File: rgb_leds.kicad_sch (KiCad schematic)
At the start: 11 parts

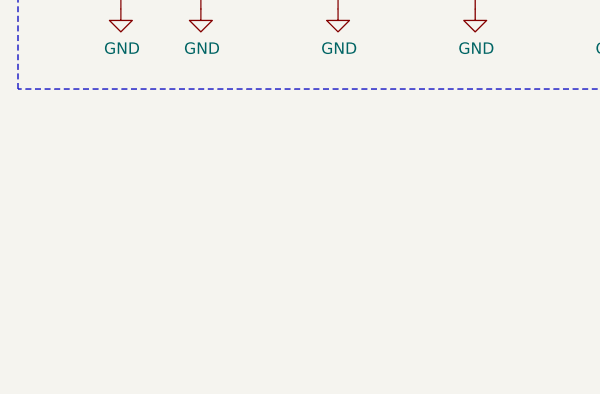
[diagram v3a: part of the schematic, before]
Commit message: Finish the board redesign with SoM on the bottom
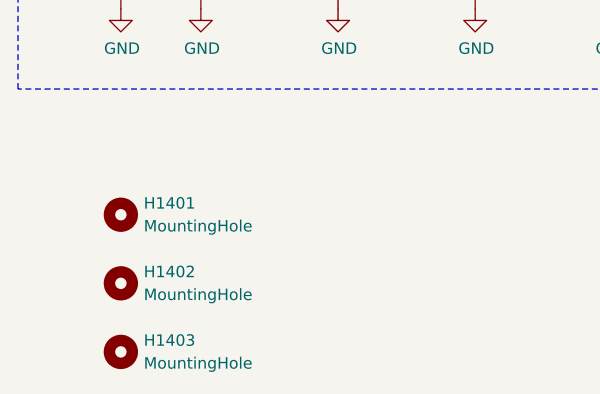
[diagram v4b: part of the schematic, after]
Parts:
- added H1401, H1402, H1403: MountingHole, MountingHole:MountingHole_3.2mm_M3, symbol Mechanical:MountingHole
- LED1401, LED1402, LED1403, LED1404, LED1405: footprint Hatlabs:LED-SMD_4P-L4.0-W1.4_SK6805SIDE-S -> Hatlabs:LED_WS2812E-4020_PLCC4_4.0x2.0mm_P0.85mm
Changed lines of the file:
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@@
 			)
 		)
-		(property "Datasheet" "https://search.murata.co.jp/Ceramy/image/img/A01X/G101/ENG/GRM155R71C104KA88-01.pdf"
+		(property "Datasheet" "~"
 			(at 121.92 120.65 0)
 			(effects
@@
 			)
 		)
-		(property "Description" ""
+		(property "Description" "Unpolarized capacitor"
 			(at 121.92 120.65 0)
 			(effects
@@
 				(path "/abc482bd-3f17-4d35-80db-1da3dcdb5c27/850df4bf-e40a-4082-adc2-76804638b949/7441bc5f-8874-43c2-af8a-50459ea25028"
 					(reference "C1403")
+					(unit 1)
+				)
+			)
+		)
+	)
+	(symbol
+		(lib_id "Mechanical:MountingHole")
+		(at 97.79 154.94 0)
+		(unit 1)
+		(exclude_from_sim no)
+		(in_bom no)
+		(on_board yes)
+		(dnp no)
+		(fields_autoplaced yes)
+		(property "Reference" "H1402"
+			(at 100.33 153.6699 0)
+			(effects
+				(font
+					(size 1.27 1.27)
+				)
+				(justify left)
+			)
+		)
+		(property "Value" "MountingHole"
+			(at 100.33 156.2099 0)
+			(effects
+				(font
+					(size 1.27 1.27)
+				)
+				(justify left)
+			)
+		)
+		(property "Footprint" "MountingHole:MountingHole_3.2mm_M3"
+			(at 97.79 154.94 0)
+			(effects
+				(font
+					(size 1.27 1.27)
+				)
+				(hide yes)
+			)
+		)
+		(property "Datasheet" "~"
+			(at 97.79 154.94 0)
+			(effects
+				(font
+					(size 1.27 1.27)
+				)
+				(hide yes)
+			)
+		)
+		(property "Description" "Mounting Hole without connection"
+			(at 97.79 154.94 0)
+			(effects
+				(font
+					(size 1.27 1.27)
+				)
+				(hide yes)
+			)
+		)
+		(instances
+			(project "HALPI2"
+				(path "/abc482bd-3f17-4d35-80db-1da3dcdb5c27/850df4bf-e40a-4082-adc2-76804638b949/7441bc5f-8874-43c2-af8a-50459ea25028"
+					(reference "H1402")
 					(unit 1)
 				)
@@
 			)
 		)
-		(property "Datasheet" "https://search.murata.co.jp/Ceramy/image/img/A01X/G101/ENG/GRM155R71C104KA88-01.pdf"
+		(property "Datasheet" "~"
 			(at 152.4 120.65 0)
 			(effects
@@
 			)
 		)
-		(property "Description" ""
+		(property "Description" "Unpolarized capacitor"
 			(at 152.4 120.65 0)
 			(effects
@@
 			)
 		)
-		(property "Datasheet" "https://search.murata.co.jp/Ceramy/image/img/A01X/G101/ENG/GRM155R71C104KA88-01.pdf"
+		(property "Datasheet" "~"
 			(at 137.16 120.65 0)
 			(effects
@@
 			)
 		)
-		(property "Description" ""
+		(property "Description" "Unpolarized capacitor"
 			(at 137.16 120.65 0)
 			(effects
@@
 			)
 		)
-		(property "Datasheet" ""
+		(property "Datasheet" "~"
 			(at 97.79 120.65 0)
 			(effects
@@
 			)
 		)
-		(property "Description" ""
+		(property "Description" "Unpolarized capacitor"
 			(at 97.79 120.65 0)
 			(effects
@@
 				(path "/abc482bd-3f17-4d35-80db-1da3dcdb5c27/850df4bf-e40a-4082-adc2-76804638b949/7441bc5f-8874-43c2-af8a-50459ea25028"
 					(reference "C1401")
+					(unit 1)
+				)
+			)
+		)
+	)
+	(symbol
+		(lib_id "Mechanical:MountingHole")
+		(at 97.79 147.32 0)
+		(unit 1)
+		(exclude_from_sim no)
+		(in_bom no)
+		(on_board yes)
+		(dnp no)
+		(fields_autoplaced yes)
+		(property "Reference" "H1401"
+			(at 100.33 146.0499 0)
+			(effects
+				(font
+					(size 1.27 1.27)
+				)
+				(justify left)
+			)
+		)
+		(property "Value" "MountingHole"
+			(at 100.33 148.5899 0)
+			(effects
+				(font
+					(size 1.27 1.27)
+				)
+				(justify left)
+			)
+		)
+		(property "Footprint" "MountingHole:MountingHole_3.2mm_M3"
+			(at 97.79 147.32 0)
+			(effects
+				(font
+					(size 1.27 1.27)
+				)
+				(hide yes)
+			)
+		)
+		(property "Datasheet" "~"
+			(at 97.79 147.32 0)
+			(effects
+				(font
+					(size 1.27 1.27)
+				)
+				(hide yes)
+			)
+		)
+		(property "Description" "Mounting Hole without connection"
+			(at 97.79 147.32 0)
+			(effects
+				(font
+					(size 1.27 1.27)
+				)
+				(hide yes)
+			)
+		)
+		(instances
+			(project ""
+				(path "/abc482bd-3f17-4d35-80db-1da3dcdb5c27/850df4bf-e40a-4082-adc2-76804638b949/7441bc5f-8874-43c2-af8a-50459ea25028"
+					(reference "H1401")
 					(unit 1)
 				)
@@
 			)
 		)
-		(property "Footprint" "Hatlabs:LED-SMD_4P-L4.0-W1.4_SK6805SIDE-S"
+		(property "Footprint" "Hatlabs:LED_WS2812E-4020_PLCC4_4.0x2.0mm_P0.85mm"
 			(at 125.73 100.33 0)
 			(effects
@@
 			)
 		)
-		(property "Datasheet" "https://www.lcsc.com/datasheet/lcsc_datasheet_2110250930_OPSCO-Optoelectronics-SK6805MICRO-J_C2909056.pdf"
+		(property "Datasheet" "https://cdn-shop.adafruit.com/datasheets/WS2812B.pdf"
 			(at 120.65 100.33 0)
 			(effects
@@
 			)
 		)
-		(property "Footprint" "Hatlabs:LED-SMD_4P-L4.0-W1.4_SK6805SIDE-S"
+		(property "Footprint" "Hatlabs:LED_WS2812E-4020_PLCC4_4.0x2.0mm_P0.85mm"
 			(at 156.21 100.33 0)
 			(effects
@@
 			)
 		)
-		(property "Datasheet" "https://www.lcsc.com/datasheet/lcsc_datasheet_2110250930_OPSCO-Optoelectronics-SK6805MICRO-J_C2909056.pdf"
+		(property "Datasheet" "https://cdn-shop.adafruit.com/datasheets/WS2812B.pdf"
 			(at 151.13 100.33 0)
 			(effects
@@
 			)
 		)
-		(property "Datasheet" "https://search.murata.co.jp/Ceramy/image/img/A01X/G101/ENG/GRM155R71C104KA88-01.pdf"
+		(property "Datasheet" "~"
 			(at 167.64 120.65 0)
 			(effects
@@
 			)
 		)
-		(property "Description" ""
+		(property "Description" "Unpolarized capacitor"
 			(at 167.64 120.65 0)
 			(effects
@@
 			)
 		)
-		(property "Datasheet" "https://search.murata.co.jp/Ceramy/image/img/A01X/G101/ENG/GRM155R71C104KA88-01.pdf"
+		(property "Datasheet" "~"
 			(at 106.68 120.65 0)
 			(effects
@@
 			)
 		)
-		(property "Description" ""
+		(property "Description" "Unpolarized capacitor"
 			(at 106.68 120.65 0)
 			(effects
@@
 			)
 		)
-		(property "Footprint" "Hatlabs:LED-SMD_4P-L4.0-W1.4_SK6805SIDE-S"
+		(property "Footprint" "Hatlabs:LED_WS2812E-4020_PLCC4_4.0x2.0mm_P0.85mm"
 			(at 140.97 100.33 0)
 			(effects
@@
 			)
 		)
-		(property "Datasheet" "https://www.lcsc.com/datasheet/lcsc_datasheet_2110250930_OPSCO-Optoelectronics-SK6805MICRO-J_C2909056.pdf"
+		(property "Datasheet" "https://cdn-shop.adafruit.com/datasheets/WS2812B.pdf"
 			(at 135.89 100.33 0)
 			(effects
@@
 			)
 		)
-		(property "Footprint" "Hatlabs:LED-SMD_4P-L4.0-W1.4_SK6805SIDE-S"
+		(property "Footprint" "Hatlabs:LED_WS2812E-4020_PLCC4_4.0x2.0mm_P0.85mm"
 			(at 171.45 100.33 0)
 			(effects
@@
 			)
 		)
-		(property "Datasheet" "https://www.lcsc.com/datasheet/lcsc_datasheet_2110250930_OPSCO-Optoelectronics-SK6805MICRO-J_C2909056.pdf"
+		(property "Datasheet" "https://cdn-shop.adafruit.com/datasheets/WS2812B.pdf"
 			(at 166.37 100.33 0)
 			(effects
@@
 			)
 		)
-		(property "Footprint" "Hatlabs:LED-SMD_4P-L4.0-W1.4_SK6805SIDE-S"
+		(property "Footprint" "Hatlabs:LED_WS2812E-4020_PLCC4_4.0x2.0mm_P0.85mm"
 			(at 110.49 100.33 0)
 			(effects
@@
 			)
 		)
-		(property "Datasheet" "https://www.lcsc.com/datasheet/lcsc_datasheet_2110250930_OPSCO-Optoelectronics-SK6805MICRO-J_C2909056.pdf"
+		(property "Datasheet" "https://cdn-shop.adafruit.com/datasheets/WS2812B.pdf"
 			(at 105.41 100.33 0)
 			(effects
@@
 					(unit 1)
 				)
+			)
+		)
+	)
+	(symbol
+		(lib_id "Mechanical:MountingHole")
+		(at 97.79 162.56 0)
+		(unit 1)
+		(exclude_from_sim no)
+		(in_bom no)
+		(on_board yes)
+		(dnp no)
+		(fields_autoplaced yes)
+		(property "Reference" "H1403"
+			(at 100.33 161.2899 0)
+			(effects
+				(font
+					(size 1.27 1.27)
+				)
+				(justify left)
+			)
+		)
+		(property "Value" "MountingHole"
+			(at 100.33 163.8299 0)
+			(effects
+				(font
+					(size 1.27 1.27)
+				)
+				(justify left)
+			)
+		)
+		(property "Footprint" "MountingHole:MountingHole_3.2mm_M3"
+			(at 97.79 162.56 0)
+			(effects
+				(font
+					(size 1.27 1.27)
+				)
+				(hide yes)
+			)
+		)
+		(property "Datasheet" "~"
+			(at 97.79 162.56 0)
+			(effects
+				(font
+					(size 1.27 1.27)
+				)
+				(hide yes)
+			)
+		)
+		(property "Description" "Mounting Hole without connection"
+			(at 97.79 162.56 0)
+			(effects
+				(font
+					(size 1.27 1.27)
+				)
+				(hide yes)
+			)
+		)
+		(instances
+			(project "HALPI2"
+				(path "/abc482bd-3f17-4d35-80db-1da3dcdb5c27/850df4bf-e40a-4082-adc2-76804638b949/7441bc5f-8874-43c2-af8a-50459ea25028"
+					(reference "H1403")
+					(unit 1)
+				)

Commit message: Further refinements
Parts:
- added TP1207: TestPoint, TestPoint:TestPoint_Pad_D1.0mm, symbol Connector:TestPoint
- LED1401, LED1402, LED1403, LED1404, LED1405: value SK6805MICRO-J -> SK6805SIDE-G-003; footprint Hatlabs:LED_WS2812E-4020_PLCC4_4.0x2.0mm_P0.85mm -> Hatlabs:LED-SMD_4P-L3.5-W1.55_SK6805SIDE-G; symbol Hatlabs:Worldsemi_WS2812E-4020 -> Hatlabs:SK6805SIDE-G; LCSC C2909057 -> C31452139
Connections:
- net +5V: now also LED1401.3 (VCC), LED1402.3 (VCC), LED1403.3 (VCC), LED1404.3 (VCC), LED1405.3 (VCC); no longer LED1401.1 (VCC), LED1402.1 (VCC), LED1403.1 (VCC), LED1404.1 (VCC), LED1405.1 (VCC)
- net DIN2: now also LED1401.1 (DOUT); no longer LED1401.2 (DOUT)
- net DIN3: now also LED1402.1 (DOUT); no longer LED1402.2 (DOUT)
- net DIN4: now also LED1403.1 (DOUT); no longer LED1403.2 (DOUT)
- net DIN5: now also LED1404.1 (DOUT); no longer LED1404.2 (DOUT)
- net GND: now also LED1401.2 (GND), LED1402.2 (GND), LED1403.2 (GND), LED1404.2 (GND), LED1405.2 (GND); no longer LED1401.3 (GND), LED1402.3 (GND), LED1403.3 (GND), LED1404.3 (GND), LED1405.3 (GND)
- new net DOUT: LED1405.1 (DOUT), TP1207.1
- no-connect marks 1 -> 0

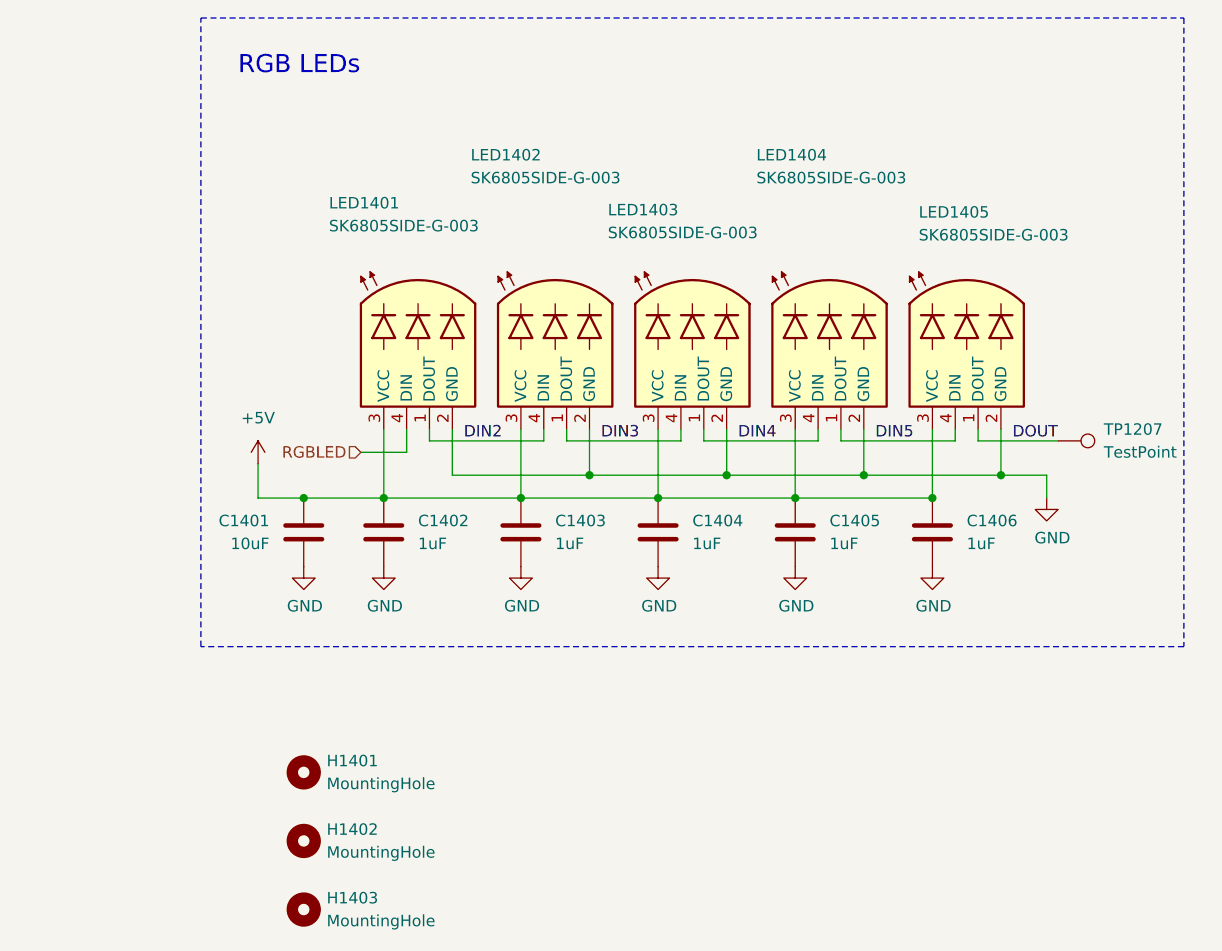
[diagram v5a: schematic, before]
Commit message: Finish transitioning to RP2040
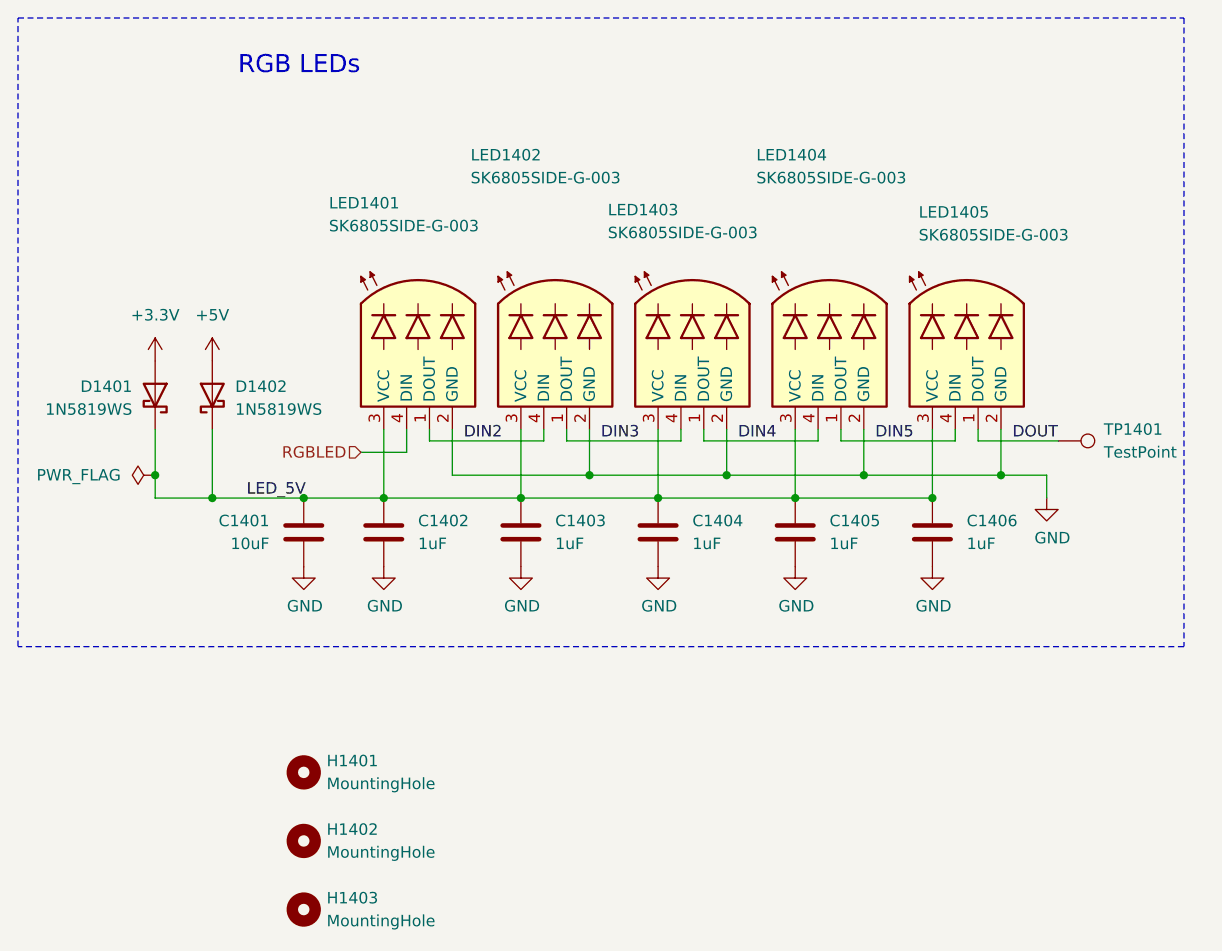
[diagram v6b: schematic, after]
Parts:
- added D1401, D1402: 1N5819WS, Diode_SMD:D_SOD-323, symbol Device:D_Schottky
- renumbered TP1207 to TP1401
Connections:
- net +5V: now also D1402.2 (A); no longer C1401.1, C1402.1, C1403.1, C1404.1, C1405.1, C1406.1, LED1401.3 (VCC), LED1402.3 (VCC), LED1403.3 (VCC), LED1404.3 (VCC), LED1405.3 (VCC)
- new net +3.3V: D1401.2 (A)
- new net LED_5V: C1401.1, C1402.1, C1403.1, C1404.1, C1405.1, C1406.1, D1401.1 (K), D1402.1 (K), LED1401.3 (VCC), LED1402.3 (VCC), LED1403.3 (VCC), LED1404.3 (VCC), LED1405.3 (VCC)

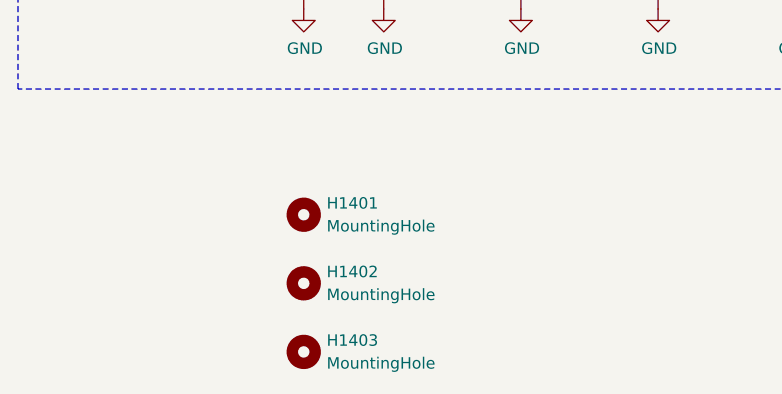
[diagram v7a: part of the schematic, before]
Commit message: Update the design to match the enclosure changes
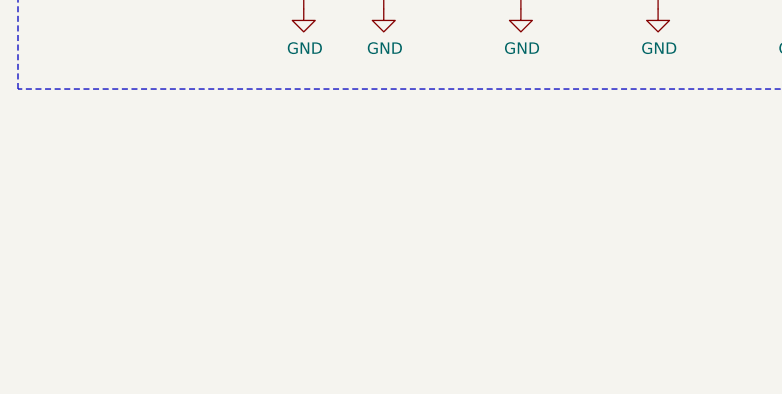
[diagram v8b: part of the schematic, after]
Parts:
- removed H1401, H1402, H1403: MountingHole, MountingHole:MountingHole_3.2mm_M3, symbol Mechanical:MountingHole
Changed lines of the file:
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@@
 	(title_block
 		(title "HALPI2")
-		(date "2025-02-26")
-		(rev "v0.1.0")
+		(date "2025-03-27")
+		(rev "v0.2.0")
 		(company "Hat Labs Oy")
 		(comment 1 "https://ohwr.org/cern_ohl_s_v2.pdf")
@@
 	)
 	(symbol
-		(lib_id "Mechanical:MountingHole")
-		(at 97.79 154.94 0)
-		(unit 1)
-		(exclude_from_sim no)
-		(in_bom no)
-		(on_board yes)
-		(dnp no)
-		(fields_autoplaced yes)
-		(property "Reference" "H1402"
-			(at 100.33 153.6699 0)
-			(effects
-				(font
-					(size 1.27 1.27)
-				)
-				(justify left)
-			)
-		)
-		(property "Value" "MountingHole"
-			(at 100.33 156.2099 0)
-			(effects
-				(font
-					(size 1.27 1.27)
-				)
-				(justify left)
-			)
-		)
-		(property "Footprint" "MountingHole:MountingHole_3.2mm_M3"
-			(at 97.79 154.94 0)
-			(effects
-				(font
-					(size 1.27 1.27)
-				)
-				(hide yes)
-			)
-		)
-		(property "Datasheet" "~"
-			(at 97.79 154.94 0)
-			(effects
-				(font
-					(size 1.27 1.27)
-				)
-				(hide yes)
-			)
-		)
-		(property "Description" "Mounting Hole without connection"
-			(at 97.79 154.94 0)
-			(effects
-				(font
-					(size 1.27 1.27)
-				)
-				(hide yes)
-			)
-		)
-		(property "LCSC Part" ""
-			(at 97.79 154.94 0)
-			(effects
-				(font
-					(size 1.27 1.27)
-				)
-			)
-		)
-		(instances
-			(project "HALPI2"
-				(path "/abc482bd-3f17-4d35-80db-1da3dcdb5c27/850df4bf-e40a-4082-adc2-76804638b949/7441bc5f-8874-43c2-af8a-50459ea25028"
-					(reference "H1402")
-					(unit 1)
-				)
-			)
-		)
-	)
-	(symbol
 		(lib_id "power:GND")
 		(at 97.79 124.46 0)
@@
 	)
 	(symbol
-		(lib_id "Mechanical:MountingHole")
-		(at 97.79 147.32 0)
-		(unit 1)
-		(exclude_from_sim no)
-		(in_bom no)
-		(on_board yes)
-		(dnp no)
-		(fields_autoplaced yes)
-		(property "Reference" "H1401"
-			(at 100.33 146.0499 0)
-			(effects
-				(font
-					(size 1.27 1.27)
-				)
-				(justify left)
-			)
-		)
-		(property "Value" "MountingHole"
-			(at 100.33 148.5899 0)
-			(effects
-				(font
-					(size 1.27 1.27)
-				)
-				(justify left)
-			)
-		)
-		(property "Footprint" "MountingHole:MountingHole_3.2mm_M3"
-			(at 97.79 147.32 0)
-			(effects
-				(font
-					(size 1.27 1.27)
-				)
-				(hide yes)
-			)
-		)
-		(property "Datasheet" "~"
-			(at 97.79 147.32 0)
-			(effects
-				(font
-					(size 1.27 1.27)
-				)
-				(hide yes)
-			)
-		)
-		(property "Description" "Mounting Hole without connection"
-			(at 97.79 147.32 0)
-			(effects
-				(font
-					(size 1.27 1.27)
-				)
-				(hide yes)
-			)
-		)
-		(property "LCSC Part" ""
-			(at 97.79 147.32 0)
-			(effects
-				(font
-					(size 1.27 1.27)
-				)
-			)
-		)
-		(instances
-			(project ""
-				(path "/abc482bd-3f17-4d35-80db-1da3dcdb5c27/850df4bf-e40a-4082-adc2-76804638b949/7441bc5f-8874-43c2-af8a-50459ea25028"
-					(reference "H1401")
-					(unit 1)
-				)
-			)
-		)
-	)
-	(symbol
 		(lib_id "power:GND")
 		(at 167.64 124.46 0)
@@
 					(unit 1)
 				)
-			)
-		)
-	)
-	(symbol
-		(lib_id "Mechanical:MountingHole")
-		(at 97.79 162.56 0)
-		(unit 1)
-		(exclude_from_sim no)
-		(in_bom no)
-		(on_board yes)
-		(dnp no)
-		(fields_autoplaced yes)
-		(property "Reference" "H1403"
-			(at 100.33 161.2899 0)
-			(effects
-				(font
-					(size 1.27 1.27)
-				)
-				(justify left)
-			)
-		)
-		(property "Value" "MountingHole"
-			(at 100.33 163.8299 0)
-			(effects
-				(font
-					(size 1.27 1.27)
-				)
-				(justify left)
-			)
-		)
-		(property "Footprint" "MountingHole:MountingHole_3.2mm_M3"
-			(at 97.79 162.56 0)
-			(effects
-				(font
-					(size 1.27 1.27)
-				)
-				(hide yes)
-			)
-		)
-		(property "Datasheet" "~"
-			(at 97.79 162.56 0)
-			(effects
-				(font
-					(size 1.27 1.27)
-				)
-				(hide yes)
-			)
-		)
-		(property "Description" "Mounting Hole without connection"
-			(at 97.79 162.56 0)
-			(effects
-				(font
-					(size 1.27 1.27)
-				)
-				(hide yes)
-			)
-		)
-		(property "LCSC Part" ""
-			(at 97.79 162.56 0)
-			(effects
-				(font
-					(size 1.27 1.27)
-				)
-			)
-		)
-		(instances
-			(project "HALPI2"
-				(path "/abc482bd-3f17-4d35-80db-1da3dcdb5c27/850df4bf-e40a-4082-adc2-76804638b949/7441bc5f-8874-43c2-af8a-50459ea25028"
-					(reference "H1403")
-					(unit 1)
-				)
